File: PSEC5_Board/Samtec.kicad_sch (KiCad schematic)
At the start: 2 parts, among them J1 QTH-040-01-X-D-DP-A, J9 QTH-040-01-X-D-DP-A

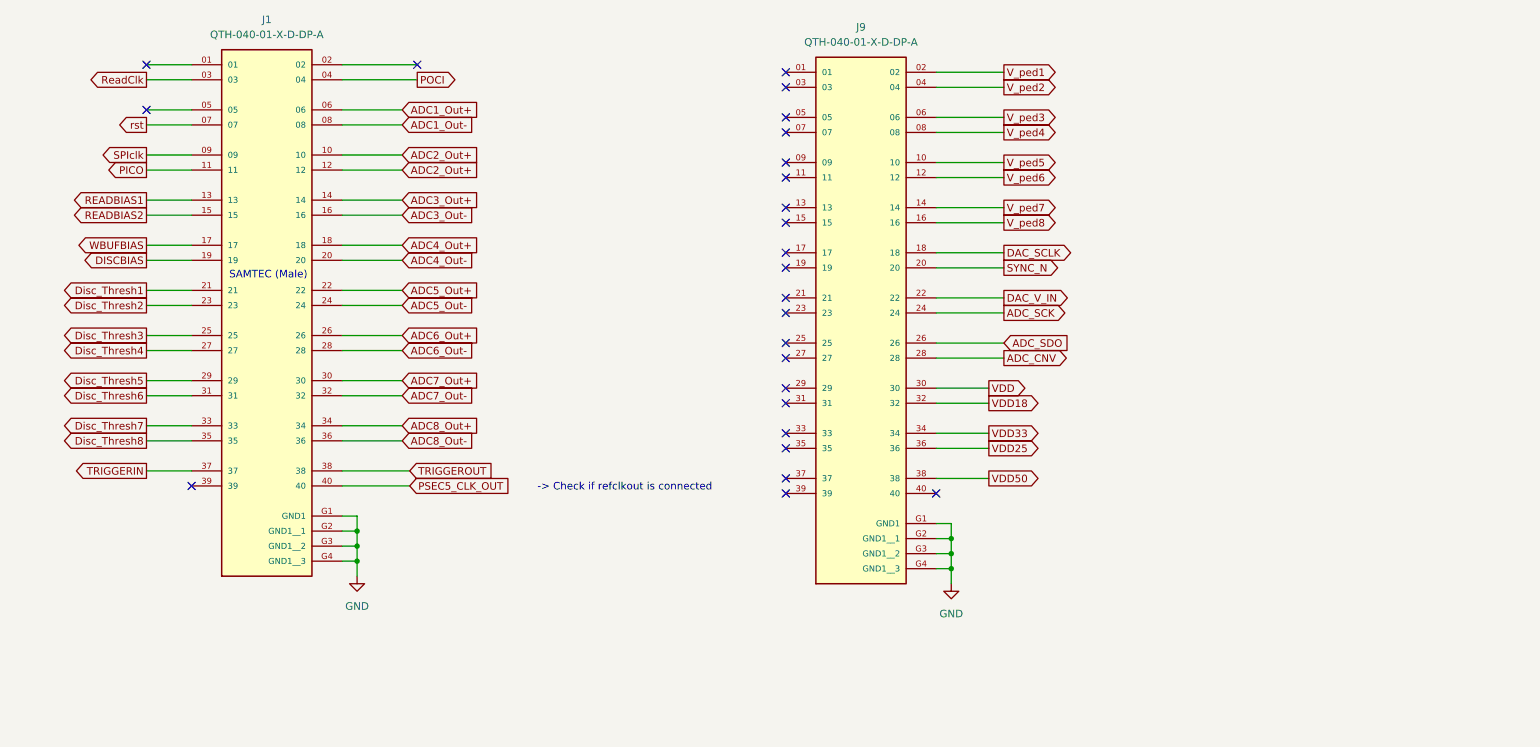
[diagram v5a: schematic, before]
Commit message: DUT Layout Overhaul
Footprints need to be replaced.
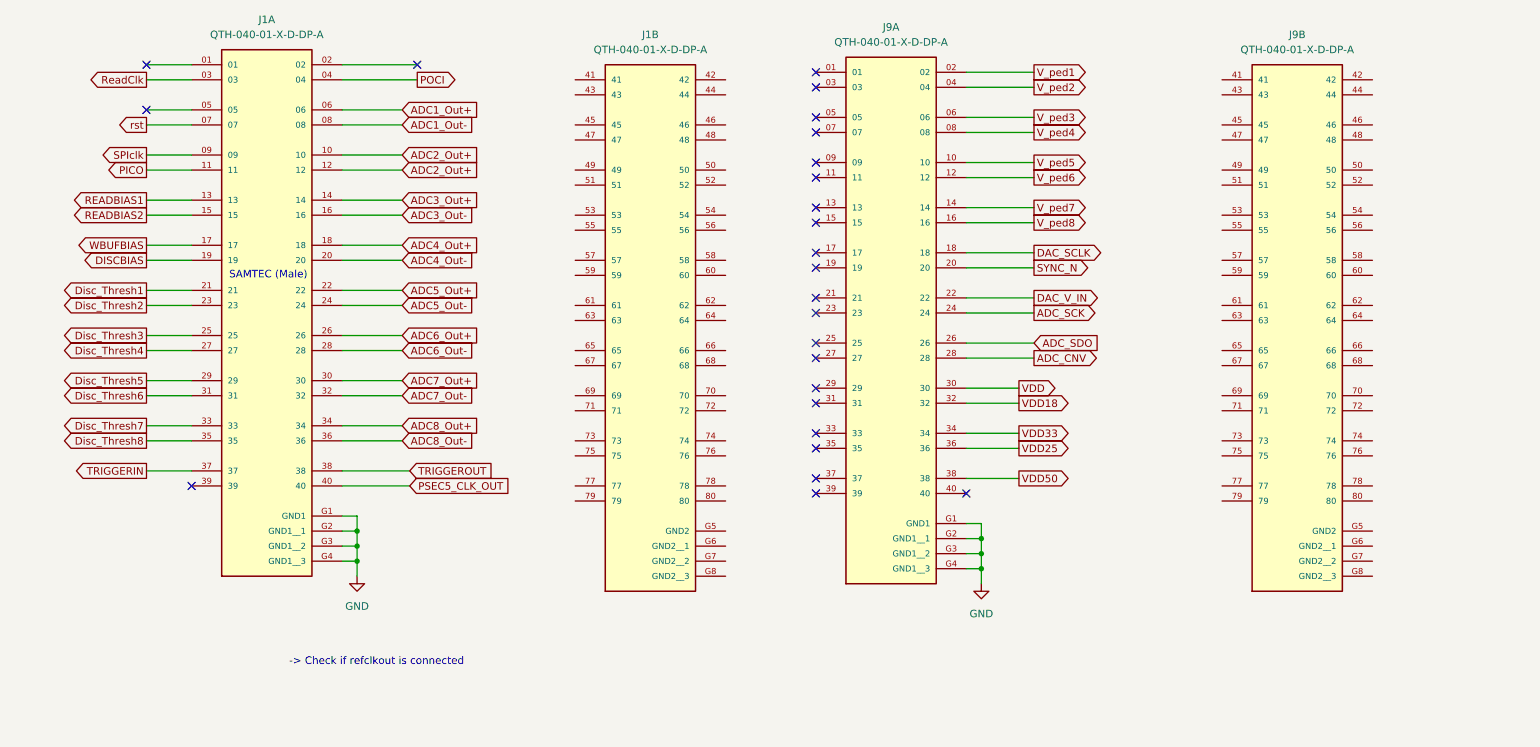
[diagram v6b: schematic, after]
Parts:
- removed J1, J9: QTH-040-01-X-D-DP-A, QTH-040-01-X-D-DP-A:SAMTEC_QTH-040-01-X-D-DP-A, symbol QTH-040-01-X-D-DP-A:QTH-040-01-X-D-DP-A
- added J1, J9: QTH-040-01-X-D-DP-A, QTH-040-01-X-D-DP-A:SAMTEC_QTH-040-01-X-D-DP-A, symbol QTH-040-01-L-D-DP-A:QTH-040-01-X-D-DP-A
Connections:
- net ADC1_Out+: now also J1.06
- net ADC1_Out-: now also J1.08
- net ADC2_Out+: now also J1.10, J1.12
- net ADC3_Out+: now also J1.14
- net ADC3_Out-: now also J1.16
- net ADC4_Out+: now also J1.18
- net ADC4_Out-: now also J1.20
- net ADC5_Out+: now also J1.22
- net ADC5_Out-: now also J1.24
- net ADC6_Out+: now also J1.26
- net ADC6_Out-: now also J1.28
- net ADC7_Out+: now also J1.30
- net ADC7_Out-: now also J1.32
- net ADC8_Out+: now also J1.34
- net ADC8_Out-: now also J1.36
- net ADC_CNV: now also J9.28
- net ADC_SCK: now also J9.24
- net ADC_SDO: now also J9.26
- net DAC_SCLK: now also J9.18
- net DAC_V_IN: now also J9.22
- net DISCBIAS: now also J1.19
- net Disc_Thresh1: now also J1.21
- net Disc_Thresh2: now also J1.23
- net Disc_Thresh3: now also J1.25
- net Disc_Thresh4: now also J1.27
- net Disc_Thresh5: now also J1.29
- net Disc_Thresh6: now also J1.31
- net Disc_Thresh7: now also J1.33
- net Disc_Thresh8: now also J1.35
- net GND: now also J1.G1 (GND1), J1.G2 (GND1__1), J1.G3 (GND1__2), J1.G4 (GND1__3), J9.G1 (GND1), J9.G2 (GND1__1), J9.G3 (GND1__2), J9.G4 (GND1__3)
- net PICO: now also J1.11
- net POCI: now also J1.04
- net PSEC5_CLK_OUT: now also J1.40
- net READBIAS1: now also J1.13
- net READBIAS2: now also J1.15
- net ReadClk: now also J1.03
- net SPIclk: now also J1.09
- net SYNC_N: now also J9.20
- net TRIGGERIN: now also J1.37
- net TRIGGEROUT: now also J1.38
- net VDD: now also J9.30
- net VDD18: now also J9.32
- net VDD25: now also J9.36
- net VDD33: now also J9.34
- net VDD50: now also J9.38
- net V_ped1: now also J9.02
- net V_ped2: now also J9.04
- net V_ped3: now also J9.06
- net V_ped4: now also J9.08
- net V_ped5: now also J9.10
- net V_ped6: now also J9.12
- net V_ped7: now also J9.14
- net V_ped8: now also J9.16
- net WBUFBIAS: now also J1.17
- net rst: now also J1.07

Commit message: DUT Layout finish 0.9
Still missing a ground plane, all other nets are connected.

Minor issue: Certain global labels are not being recognized: PSEC5_CLK_OUT
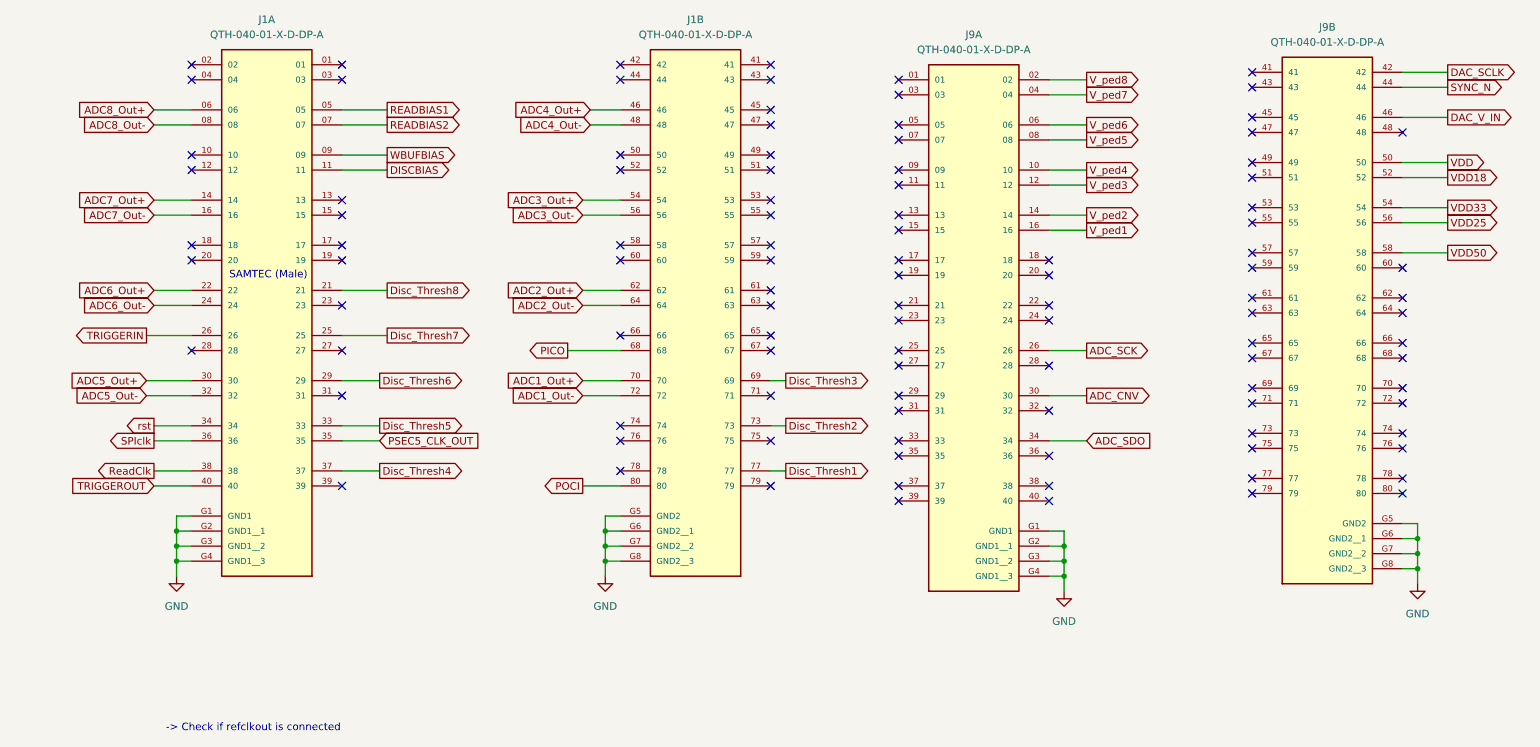
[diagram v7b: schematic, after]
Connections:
- net ADC1_Out+: now also J1.70; no longer J1.06
- net ADC1_Out-: now also J1.72; no longer J1.08
- net ADC2_Out+: now also J1.62; no longer J1.10, J1.12
- net ADC3_Out+: now also J1.54; no longer J1.14
- net ADC3_Out-: now also J1.56; no longer J1.16
- net ADC4_Out+: now also J1.46; no longer J1.18
- net ADC4_Out-: now also J1.48; no longer J1.20
- net ADC5_Out+: now also J1.30; no longer J1.22
- net ADC5_Out-: now also J1.32; no longer J1.24
- net ADC6_Out+: now also J1.22; no longer J1.26
- net ADC6_Out-: now also J1.24; no longer J1.28
- net ADC7_Out+: now also J1.14; no longer J1.30
- net ADC7_Out-: now also J1.16; no longer J1.32
- net ADC8_Out+: now also J1.06; no longer J1.34
- net ADC8_Out-: now also J1.08; no longer J1.36
- net ADC_CNV: now also J9.30; no longer J9.28
- net ADC_SCK: now also J9.26; no longer J9.24
- net ADC_SDO: now also J9.34; no longer J9.26
- net DAC_SCLK: now also J9.42; no longer J9.18
- net DAC_V_IN: now also J9.46; no longer J9.22
- net DISCBIAS: now also J1.11; no longer J1.19
- net Disc_Thresh1: now also J1.77; no longer J1.21
- net Disc_Thresh2: now also J1.73; no longer J1.23
- net Disc_Thresh3: now also J1.69; no longer J1.25
- net Disc_Thresh4: now also J1.37; no longer J1.27
- net Disc_Thresh5: now also J1.33; no longer J1.29
- net Disc_Thresh6: now also J1.29; no longer J1.31
- net Disc_Thresh7: now also J1.25; no longer J1.33
- net Disc_Thresh8: now also J1.21; no longer J1.35
- net GND: now also J1.G5 (GND2), J1.G6 (GND2__1), J1.G7 (GND2__2), J1.G8 (GND2__3), J9.G5 (GND2), J9.G6 (GND2__1), J9.G7 (GND2__2), J9.G8 (GND2__3)
- net PICO: now also J1.68; no longer J1.11
- net POCI: now also J1.80; no longer J1.04
- net PSEC5_CLK_OUT: now also J1.35; no longer J1.40
- net READBIAS1: now also J1.05; no longer J1.13
- net READBIAS2: now also J1.07; no longer J1.15
- net ReadClk: now also J1.38; no longer J1.03
- net SPIclk: now also J1.36; no longer J1.09
- net SYNC_N: now also J9.44; no longer J9.20
- net TRIGGERIN: now also J1.26; no longer J1.37
- net TRIGGEROUT: now also J1.40; no longer J1.38
- net VDD: now also J9.50; no longer J9.30
- net VDD18: now also J9.52; no longer J9.32
- net VDD25: now also J9.56; no longer J9.36
- net VDD33: now also J9.54; no longer J9.34
- net VDD50: now also J9.58; no longer J9.38
- net V_ped1: now also J9.16; no longer J9.02
- net V_ped2: now also J9.14; no longer J9.04
- net V_ped3: now also J9.12; no longer J9.06
- net V_ped4: now also J9.10; no longer J9.08
- net V_ped5: now also J9.08; no longer J9.10
- net V_ped6: now also J9.06; no longer J9.12
- net V_ped7: now also J9.04; no longer J9.14
- net V_ped8: now also J9.02; no longer J9.16
- net WBUFBIAS: now also J1.09; no longer J1.17
- net rst: now also J1.34; no longer J1.07
- net ADC2_Out-: now reaches J1.64
- no-connect marks 25 -> 105
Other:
- moved on the sheet: J1B, J9A, J9B

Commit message: changes to layout
Made board 6 layers and starting to re-route tracks on layout design
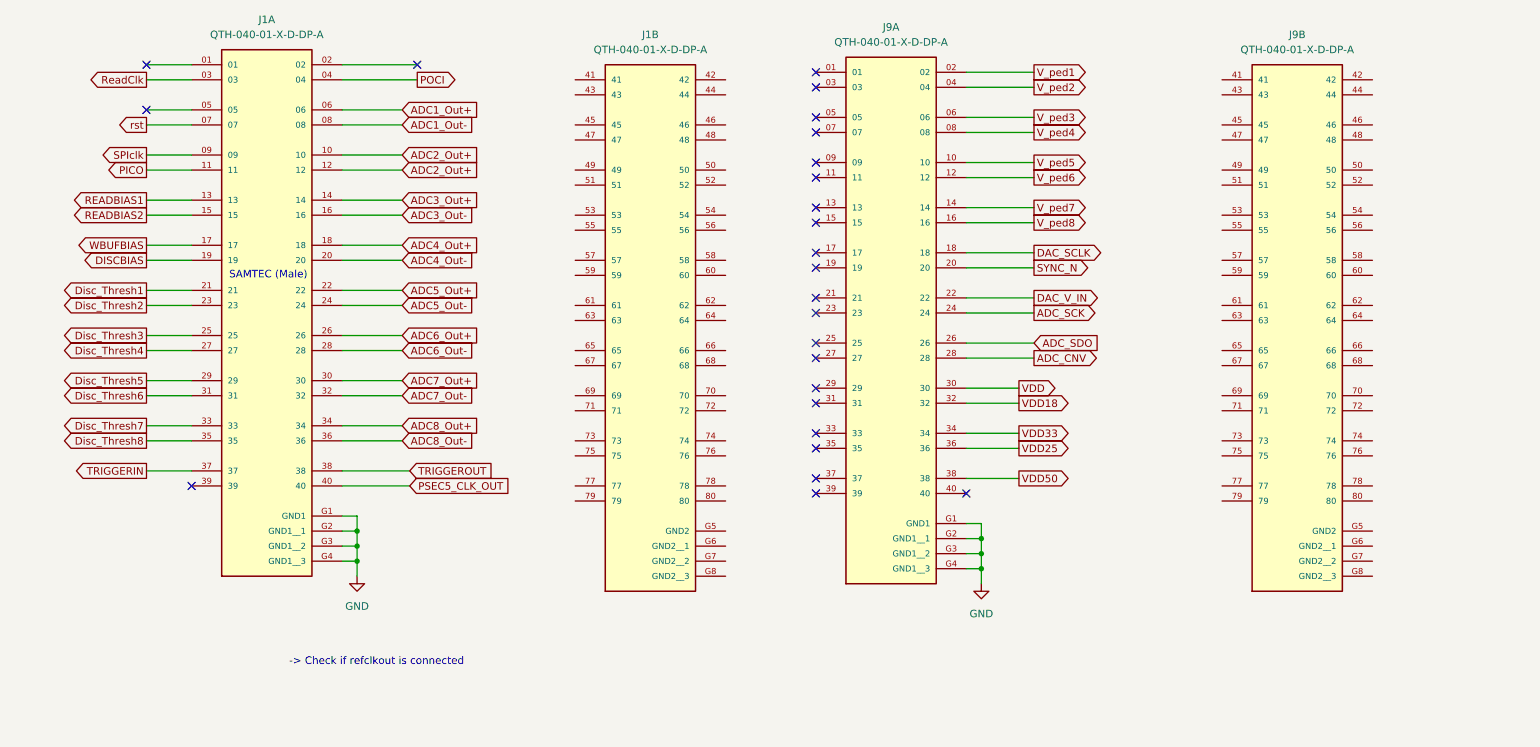
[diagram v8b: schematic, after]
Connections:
- net ADC1_Out+: now also J1.06; no longer J1.70
- net ADC1_Out-: now also J1.08; no longer J1.72
- net ADC2_Out+: now also J1.10, J1.12; no longer J1.62
- net ADC3_Out+: now also J1.14; no longer J1.54
- net ADC3_Out-: now also J1.16; no longer J1.56
- net ADC4_Out+: now also J1.18; no longer J1.46
- net ADC4_Out-: now also J1.20; no longer J1.48
- net ADC5_Out+: now also J1.22; no longer J1.30
- net ADC5_Out-: now also J1.24; no longer J1.32
- net ADC6_Out+: now also J1.26; no longer J1.22
- net ADC6_Out-: now also J1.28; no longer J1.24
- net ADC7_Out+: now also J1.30; no longer J1.14
- net ADC7_Out-: now also J1.32; no longer J1.16
- net ADC8_Out+: now also J1.34; no longer J1.06
- net ADC8_Out-: now also J1.36; no longer J1.08
- net ADC_CNV: now also J9.28; no longer J9.30
- net ADC_SCK: now also J9.24; no longer J9.26
- net ADC_SDO: now also J9.26; no longer J9.34
- net DAC_SCLK: now also J9.18; no longer J9.42
- net DAC_V_IN: now also J9.22; no longer J9.46
- net DISCBIAS: now also J1.19; no longer J1.11
- net Disc_Thresh1: now also J1.21; no longer J1.77
- net Disc_Thresh2: now also J1.23; no longer J1.73
- net Disc_Thresh3: now also J1.25; no longer J1.69
- net Disc_Thresh4: now also J1.27; no longer J1.37
- net Disc_Thresh5: now also J1.29; no longer J1.33
- net Disc_Thresh6: now also J1.31; no longer J1.29
- net Disc_Thresh7: now also J1.33; no longer J1.25
- net Disc_Thresh8: now also J1.35; no longer J1.21
- net GND: no longer J1.G5 (GND2), J1.G6 (GND2__1), J1.G7 (GND2__2), J1.G8 (GND2__3), J9.G5 (GND2), J9.G6 (GND2__1), J9.G7 (GND2__2), J9.G8 (GND2__3)
- net PICO: now also J1.11; no longer J1.68
- net POCI: now also J1.04; no longer J1.80
- net PSEC5_CLK_OUT: now also J1.40; no longer J1.35
- net READBIAS1: now also J1.13; no longer J1.05
- net READBIAS2: now also J1.15; no longer J1.07
- net ReadClk: now also J1.03; no longer J1.38
- net SPIclk: now also J1.09; no longer J1.36
- net SYNC_N: now also J9.20; no longer J9.44
- net TRIGGERIN: now also J1.37; no longer J1.26
- net TRIGGEROUT: now also J1.38; no longer J1.40
- net VDD: now also J9.30; no longer J9.50
- net VDD18: now also J9.32; no longer J9.52
- net VDD25: now also J9.36; no longer J9.56
- net VDD33: now also J9.34; no longer J9.54
- net VDD50: now also J9.38; no longer J9.58
- net V_ped1: now also J9.02; no longer J9.16
- net V_ped2: now also J9.04; no longer J9.14
- net V_ped3: now also J9.06; no longer J9.12
- net V_ped4: now also J9.08; no longer J9.10
- net V_ped5: now also J9.10; no longer J9.08
- net V_ped6: now also J9.12; no longer J9.06
- net V_ped7: now also J9.14; no longer J9.04
- net V_ped8: now also J9.16; no longer J9.02
- net WBUFBIAS: now also J1.17; no longer J1.09
- net rst: now also J1.07; no longer J1.34
- net ADC2_Out-: no longer names the net of J1.64
- no-connect marks 105 -> 25
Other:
- moved on the sheet: J1B, J9A, J9B
